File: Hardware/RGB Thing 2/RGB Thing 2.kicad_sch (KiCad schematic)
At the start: 9 parts, among them J1 JST_SH_BM048, J2 UPDI Connection, U1 ATtiny1617

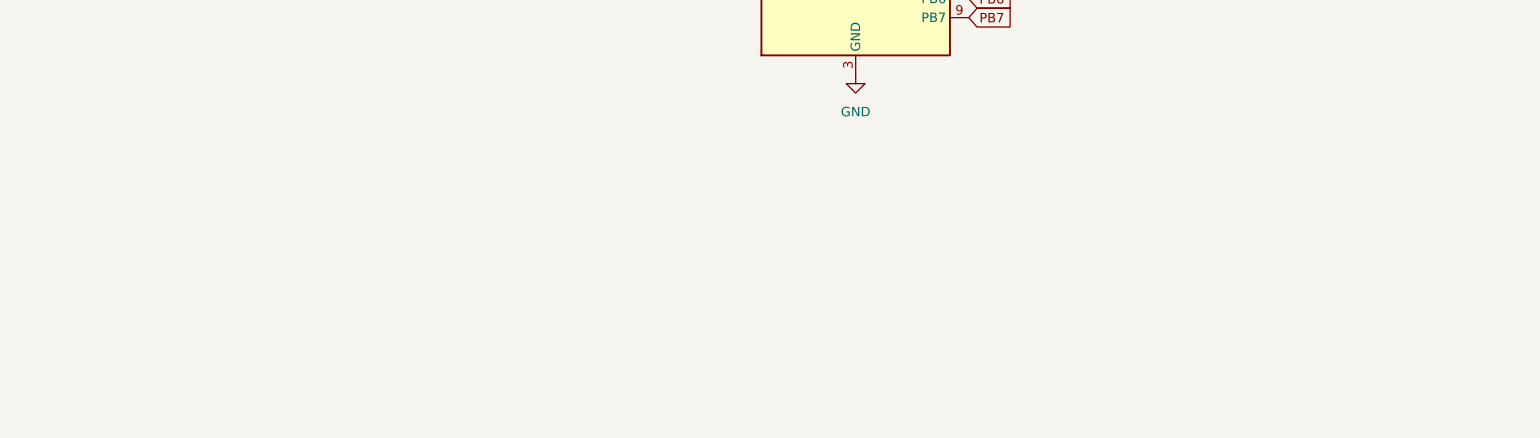
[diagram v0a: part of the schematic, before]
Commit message: Eliminated useless test points... and... NOW WITH RGB!!!
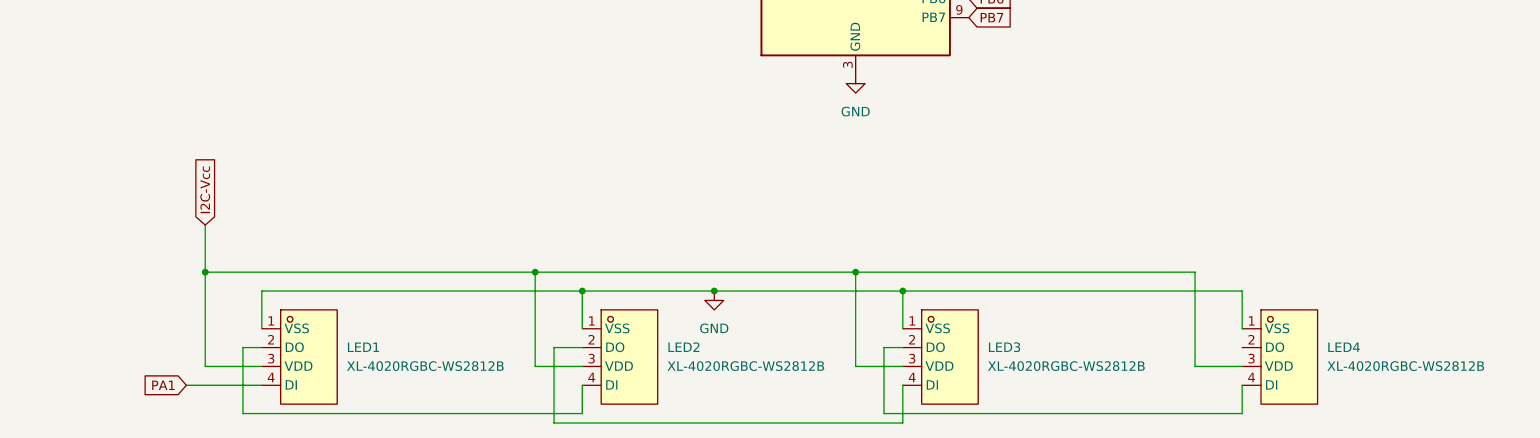
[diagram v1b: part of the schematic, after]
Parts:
- added LED1, LED2, LED3, LED4: XL-4020RGBC-WS2812B, tinker:LED-SMD_4P-L4.0-W1.7_XL-4020RGBC-WS2812B, symbol New_Library:XL-4020RGBC-WS2812B
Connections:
- net GND: now also LED1.1 (VSS), LED2.1 (VSS), LED3.1 (VSS), LED4.1 (VSS)
- net I2C-Vcc: now also LED1.3 (VDD), LED2.3 (VDD), LED3.3 (VDD), LED4.3 (VDD)
- net PA1: now also LED1.4 (DI)
- new net: LED1.2 (DO), LED2.4 (DI)
- new net: LED2.2 (DO), LED3.4 (DI)
- new net: LED3.2 (DO), LED4.4 (DI)
